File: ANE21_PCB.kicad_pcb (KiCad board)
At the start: 4 copper layers, 74.6 x 59.6 mm, 60 parts, among them J1 Conn_02x05_Odd_Even, J13 1-2199119-5, J15 USB_OTG, J16 Conn_01x02, J2 Barrel_Jack, J3 USB-A-S-VT, J4 THD-20-R, J5 690-019-298-412, J6 SS-52400-004, U1 74LVC1G07SE-7, U10 PUSB3FR4, U11 TPD4EUSB30, U12 SI-51005-F, U13 RT9742SNGV, U2 74LVC1G07SE-7, U3 HUSB238_xxxDD, U4 AP62300WU-7, U8 AP62300WU-7, U9 PUSB3FR4

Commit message: heb de GPIO aangepast.
Laten we morgen de stand van zaken bespreken. En overleggen wat we kunnen doen
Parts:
- added R7: 10k, Resistor_SMD:R_0402_1005Metric_Pad0.72x0.64mm_HandSolder, F.Cu at (1.14, 0.49)
- moved J4 225.2 mm to (117.7, 130.5), turned to -90 degrees
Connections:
- J4 pad 1: +3,3V DC -> 3.3V OUT (CM4.84)
- J4 pad 10: /CM4_LowSpeed/GPIO15 -> /CM4_LowSpeed/GPIO7
- J4 pad 11: /CM4_LowSpeed/GPIO17 -> /CM4_LowSpeed/GPIO8
- J4 pad 12: /CM4_LowSpeed/GPIO18 -> /CM4_LowSpeed/GPIO9
- J4 pad 13: /CM4_LowSpeed/GPIO27 -> /CM4_LowSpeed/GPIO10
- J4 pad 14: GND -> /CM4_LowSpeed/GPIO11
- J4 pad 15: /CM4_LowSpeed/GPIO22 -> /CM4_LowSpeed/GPIO12
- J4 pad 16: /CM4_LowSpeed/GPIO23 -> /CM4_LowSpeed/GPIO13
- J4 pad 17: +3,3V DC -> /CM4_LowSpeed/GPIO14
- J4 pad 18: /CM4_LowSpeed/GPIO24 -> /CM4_LowSpeed/GPIO15
- J4 pad 19: /CM4_LowSpeed/GPIO10 -> /CM4_LowSpeed/GPIO16
- J4 pad 2: /CM4_LowSpeed/+5v -> 1.8V OUT (CM4.90)
- J4 pad 20: GND -> /CM4_LowSpeed/GPIO17
- J4 pad 21: /CM4_LowSpeed/GPIO9 -> /CM4_LowSpeed/GPIO18
- J4 pad 22: /CM4_LowSpeed/GPIO25 -> /CM4_LowSpeed/GPIO19
- J4 pad 23: /CM4_LowSpeed/GPIO11 -> /CM4_LowSpeed/GPIO20
- J4 pad 24: /CM4_LowSpeed/GPIO8 -> /CM4_LowSpeed/GPIO21
- J4 pad 25: GND -> /CM4_LowSpeed/GPIO22
- J4 pad 26: /CM4_LowSpeed/GPIO7 -> /CM4_LowSpeed/GPIO23
- J4 pad 27: /CM4_LowSpeed/ID_SD -> /CM4_LowSpeed/GPIO24
- J4 pad 28: /CM4_LowSpeed/ID_SC -> /CM4_LowSpeed/GPIO25
- J4 pad 29: /CM4_LowSpeed/GPIO5 -> /CM4_LowSpeed/GPIO26
- J4 pad 3: /CM4_LowSpeed/GPIO2 -> 3.3V OUT (CM4.86)
- J4 pad 30: GND -> /CM4_LowSpeed/GPIO27
- J4 pad 31: /CM4_LowSpeed/GPIO6 -> /CM4_LowSpeed/WL_nDis
- J4 pad 32: /CM4_LowSpeed/GPIO12 -> unconnected-(J4-Pin_32-Pad32)
- J4 pad 33: /CM4_LowSpeed/GPIO13 -> /CM4_LowSpeed/BT_nDis
- J4 pad 34: GND -> unconnected-(J4-Pin_34-Pad34)
- J4 pad 35: /CM4_LowSpeed/GPIO19 -> /CM4_LowSpeed/nRPIBOOT
- J4 pad 36: /CM4_LowSpeed/GPIO16 -> unconnected-(J4-Pin_36-Pad36)
- J4 pad 37: /CM4_LowSpeed/GPIO26 -> /CM4_LowSpeed/ID_SD
- J4 pad 38: /CM4_LowSpeed/GPIO20 -> /CM4_LowSpeed/ID_SC
- J4 pad 4: /CM4_LowSpeed/+5v -> 1.8V OUT (CM4.88)
- J4 pad 40: /CM4_LowSpeed/GPIO21 -> GND
- J4 pad 5: /CM4_LowSpeed/GPIO3 -> /CM4_LowSpeed/GPIO2
- J4 pad 6: GND -> /CM4_LowSpeed/GPIO3
- J4 pad 8: /CM4_LowSpeed/GPIO14 -> /CM4_LowSpeed/GPIO5
- J4 pad 9: GND -> /CM4_LowSpeed/GPIO6
- Module1 pad 20: unconnected-(Module1A-EEPROM_nWP-Pad20) -> Net-(Module1A-EEPROM_nWP)
- Module1 pad 24: unconnected-(Module1A-GPIO26-Pad24) -> /CM4_LowSpeed/GPIO26
- Module1 pad 25: unconnected-(Module1A-GPIO21-Pad25) -> /CM4_LowSpeed/GPIO21
- Module1 pad 26: unconnected-(Module1A-GPIO19-Pad26) -> /CM4_LowSpeed/GPIO19
- Module1 pad 27: unconnected-(Module1A-GPIO20-Pad27) -> /CM4_LowSpeed/GPIO20
- Module1 pad 28: unconnected-(Module1A-GPIO13-Pad28) -> /CM4_LowSpeed/GPIO13
- Module1 pad 29: unconnected-(Module1A-GPIO16-Pad29) -> /CM4_LowSpeed/GPIO16
- Module1 pad 30: unconnected-(Module1A-GPIO6-Pad30) -> /CM4_LowSpeed/GPIO6
- Module1 pad 31: unconnected-(Module1A-GPIO12-Pad31) -> /CM4_LowSpeed/GPIO12
- Module1 pad 34: unconnected-(Module1A-GPIO5-Pad34) -> /CM4_LowSpeed/GPIO5
- Module1 pad 35: unconnected-(Module1A-ID_SC-Pad35) -> /CM4_LowSpeed/ID_SC
- Module1 pad 36: unconnected-(Module1A-ID_SD-Pad36) -> /CM4_LowSpeed/ID_SD
- Module1 pad 37: unconnected-(Module1A-GPIO7-Pad37) -> /CM4_LowSpeed/GPIO7
- Module1 pad 38: unconnected-(Module1A-GPIO11-Pad38) -> /CM4_LowSpeed/GPIO11
- Module1 pad 39: unconnected-(Module1A-GPIO8-Pad39) -> /CM4_LowSpeed/GPIO8
- Module1 pad 40: unconnected-(Module1A-GPIO9-Pad40) -> /CM4_LowSpeed/GPIO9
- Module1 pad 41: unconnected-(Module1A-GPIO25-Pad41) -> /CM4_LowSpeed/GPIO25
- Module1 pad 44: unconnected-(Module1A-GPIO10-Pad44) -> /CM4_LowSpeed/GPIO10
- Module1 pad 45: unconnected-(Module1A-GPIO24-Pad45) -> /CM4_LowSpeed/GPIO24
- Module1 pad 46: unconnected-(Module1A-GPIO22-Pad46) -> /CM4_LowSpeed/GPIO22
- Module1 pad 47: unconnected-(Module1A-GPIO23-Pad47) -> /CM4_LowSpeed/GPIO23
- Module1 pad 48: unconnected-(Module1A-GPIO27-Pad48) -> /CM4_LowSpeed/GPIO27
- Module1 pad 49: unconnected-(Module1A-GPIO18-Pad49) -> /CM4_LowSpeed/GPIO18
- Module1 pad 50: unconnected-(Module1A-GPIO17-Pad50) -> /CM4_LowSpeed/GPIO17
- Module1 pad 51: unconnected-(Module1A-GPIO15-Pad51) -> /CM4_LowSpeed/GPIO15
- Module1 pad 54: unconnected-(Module1A-GPIO4-Pad54) -> /CM4_LowSpeed/GPIO4
- Module1 pad 55: unconnected-(Module1A-GPIO14-Pad55) -> /CM4_LowSpeed/GPIO14
- Module1 pad 56: unconnected-(Module1A-GPIO3-Pad56) -> /CM4_LowSpeed/GPIO3
- Module1 pad 58: unconnected-(Module1A-GPIO2-Pad58) -> /CM4_LowSpeed/GPIO2
- Module1 pad 84: +3,3V DC -> 3.3V OUT (CM4.84)
- Module1 pad 86: +3,3V DC -> 3.3V OUT (CM4.86)
- Module1 pad 88: /CM4_LowSpeed/+1.8v -> 1.8V OUT (CM4.88)
- Module1 pad 90: /CM4_LowSpeed/+1.8v -> 1.8V OUT (CM4.90)

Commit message: Added HDMI traces but have not checked them
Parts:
- moved R7 129.8 mm to (75.3, 107.0)
- moved C14 45.8 mm to (118.6, 76.8)
- moved R15 0.74 mm to (131.4, 81.2), turned to 0 degrees
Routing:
- net /CM4_LowSpeed/E7: track 0.00 -> 11.2 mm
- net /CM4_LowSpeed/E5: track 0.00 -> 10.7 mm
- net /CM4_HighSpeed/HDMI0_D2_P: track 0.00 -> 10.6 mm
- net /CM4_HighSpeed/HDMI0_D2_N: track 0.00 -> 10.6 mm
- net /CM4_LowSpeed/E2: track 0.00 -> 10.5 mm
- net /CM4_LowSpeed/E4: track 0.00 -> 10.3 mm
- net /CM4_HighSpeed/HDMI0_D1_P: track 0.00 -> 10.1 mm
- net /CM4_HighSpeed/HDMI0_D1_N: track 0.00 -> 10.1 mm
- net /CM4_HighSpeed/HDMI0_D0_P: track 0.00 -> 9.91 mm
- net /CM4_HighSpeed/HDMI0_D0_N: track 0.00 -> 9.91 mm
- net /CM4_HighSpeed/HDMI0_CK_P: track 0.00 -> 9.78 mm
- net /CM4_HighSpeed/HDMI0_CK_N: track 0.00 -> 9.78 mm
- net /CM4_LowSpeed/E8: track 0.00 -> 8.95 mm
- net /CM4_LowSpeed/E6: track 0.00 -> 8.52 mm
- net /CM4_LowSpeed/E1: track 0.00 -> 7.71 mm
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
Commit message: Added lots and lots of traces in PCB design.
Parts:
- removed J4: THD-20-R, Connector_PinHeader_2.54mm:PinHeader_2x20_P2.54mm_Vertical
- removed J6: SS-52400-004, SS-52400-004 (USB-c connector):STEWART_SS-52400-004 (USB-C)
- added J7: 2036150003 (USB-C_Connector), USB-C:CONN_2036150003_MOL(USB-c_connector), F.Cu at (115.1, 53.1)
- moved C3 85.9 mm to (108.4, 58.2), turned to 90 degrees
- moved C2 84.7 mm to (107.3, 58.2), turned to 90 degrees
- moved C1 83.4 mm to (106.3, 58.2), turned to 90 degrees
- moved U3 80.0 mm to (107.0, 55.3), turned to 180 degrees
- moved R1 78.7 mm to (103.6, 54.1), turned to 90 degrees
- moved R2 78.6 mm to (103.6, 56.5), turned to -90 degrees
- moved J3 30.9 mm to (120.7, 82.1), turned to 90 degrees
- moved U11 21.7 mm to (117.6, 77.8)
- moved C14 18.5 mm to (119.1, 58.3), turned to 180 degrees
- moved J15 16.7 mm to (130.0, 78.3)
- moved J2 13.0 mm to (129.3, 61.5), turned to 180 degrees
- moved J16 12.2 mm to (131.1, 71.5), turned to -90 degrees
- moved U9 8.93 mm to (128.2, 90.0)
- moved U12 8.88 mm to (126.0, 105.8)
- moved R15 8.87 mm to (131.6, 90.1)
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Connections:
- net /CM4_LowSpeed/E1 renamed /CM4_LowSpeed/TRD0_P
- net /CM4_LowSpeed/E10 renamed /CM4_LowSpeed/LEDY
- net /CM4_LowSpeed/E2 renamed /CM4_LowSpeed/TRD0_N
- net /CM4_LowSpeed/E5 renamed /CM4_LowSpeed/TRD2_P
- net /CM4_LowSpeed/E6 renamed /CM4_LowSpeed/TRD2_N
- net /CM4_LowSpeed/E7 renamed /CM4_LowSpeed/TRD3_P
- net /CM4_LowSpeed/E8 renamed /CM4_LowSpeed/TRD3_N
- net /CM4_LowSpeed/E9 renamed /CM4_LowSpeed/LEDG
- J13 pad 50: +3,3V DC -> /CM4_HighSpeed/P_RST
- J13 pad 52: +3,3V DC -> /CM4_HighSpeed/P_CLKnREQ
- Module1 pad 102: +3,3V DC -> /CM4_HighSpeed/P_CLKnREQ
- Module1 pad 109: +3,3V DC -> /CM4_HighSpeed/P_RST
- Module1 pad 4: /CM4_LowSpeed/E3 -> /CM4_LowSpeed/TRD1_N
- Module1 pad 6: /CM4_LowSpeed/E4 -> /CM4_LowSpeed/TRD1_P
- U12 pad 4: /CM4_LowSpeed/E3 -> /CM4_LowSpeed/TRD1_P
- U12 pad 5: /CM4_LowSpeed/E4 -> /CM4_LowSpeed/TRD1_N
- U9 pad 1: /CM4_LowSpeed/E4 -> /CM4_LowSpeed/TRD1_N
- U9 pad 10: /CM4_LowSpeed/E4 -> /CM4_LowSpeed/TRD1_N
- U9 pad 2: /CM4_LowSpeed/E3 -> /CM4_LowSpeed/TRD1_P
- U9 pad 9: /CM4_LowSpeed/E3 -> /CM4_LowSpeed/TRD1_P
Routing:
- net +3,3V DC: track 0.00 -> 124.0 mm, vias 0 -> 3
- net /CM4_LowSpeed/TRD1_N: track 0.00 -> 72.6 mm
- net /CM4_LowSpeed/TRD1_P: track 0.00 -> 70.1 mm
- net /CM4_LowSpeed/LEDG: track 0.00 -> 63.0 mm, vias 0 -> 2
- net USB_OTG: track 0.00 -> 59.4 mm, vias 0 -> 2
- net /CM4_LowSpeed/TRD2_N: track 8.52 -> 67.0 mm, vias 0 -> 1
- net /CM4_LowSpeed/TRD2_P: track 10.7 -> 67.4 mm, vias 0 -> 1
- net +5V DC: track 0.00 -> 56.6 mm, vias 0 -> 5
- net /CM4_LowSpeed/TRD0_P: track 7.71 -> 62.4 mm, vias 0 -> 1
- net VIN_U9: track 0.00 -> 54.5 mm, vias 0 -> 4
- net /CM4_LowSpeed/TRD3_P: track 11.2 -> 64.7 mm
- net /CM4_LowSpeed/TRD3_N: track 8.95 -> 61.8 mm
- net /CM4_LowSpeed/TRD0_N: track 10.5 -> 61.8 mm, vias 0 -> 1
- net GND: track 0.00 -> 49.7 mm, vias 0 -> 34
- net /CM4_LowSpeed/LEDY: track 0.00 -> 42.3 mm
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- added copper zone on In2.Cu, net +5V DC
- added copper zone on In1.Cu, net GND
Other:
- board size 74.6 x 59.6 mm -> 74.6 x 59.4 mm

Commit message: PCB is af. kan je het nog checken?
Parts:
- moved J1 92.0 mm to (62.9, 112.5), turned to 90 degrees
- moved U1 72.2 mm to (63.5, 106.7), turned to 180 degrees
- moved R23 0.43 mm to (86.1, 105.5)
- moved D3 0.28 mm to (85.7, 107.0)
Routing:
- net GND: track 49.7 -> 459.5 mm, vias 34 -> 45
- net +3,3V DC: track 124.0 -> 204.9 mm, vias 3 -> 4
- net +5V DC: track 56.6 -> 89.6 mm
- net Net-(J1-Pin_1): track 0.00 -> 8.06 mm
- net Net-(D3-K): track 4.19 -> 4.77 mm
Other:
- board size 74.6 x 59.4 mm -> 74.6 x 66 mm

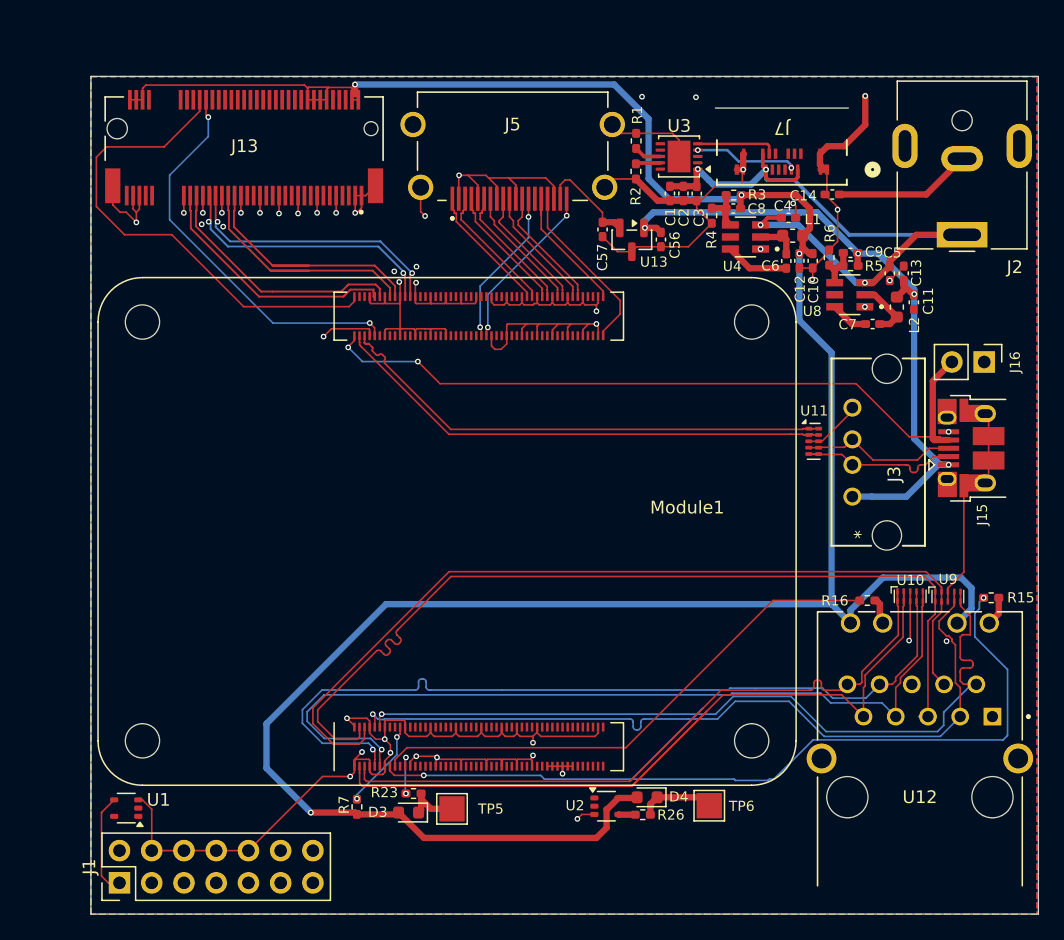
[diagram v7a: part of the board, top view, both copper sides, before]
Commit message: Redid the routing and fixed ERC warnings
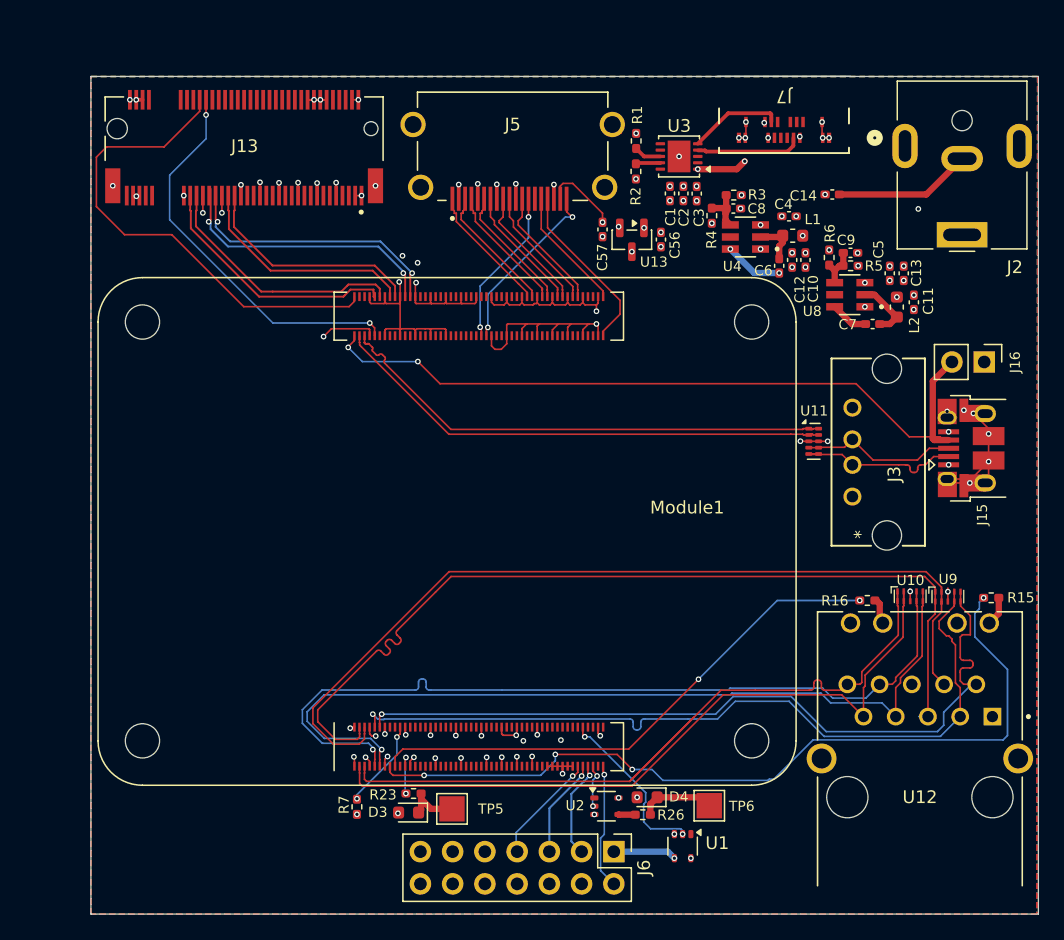
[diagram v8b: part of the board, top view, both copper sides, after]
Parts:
- removed J1: Conn_02x05_Odd_Even, Connector_PinHeader_2.54mm:PinHeader_2x07_P2.54mm_Vertical
- added J6: Conn_02x07_Odd_Even, Connector_PinHeader_2.54mm:PinHeader_2x07_P2.54mm_Vertical, F.Cu at (101.9, 110.1)
- moved U1 43.9 mm to (107.3, 109.6), turned to -90 degrees
- moved J7 2.50 mm to (115.3, 50.6)
- moved C6 0.67 mm to (114.9, 63.9)
- moved C10 0.57 mm to (117.0, 63.5)
- moved C12 0.57 mm to (115.9, 63.5)
- moved C4 0.14 mm to (115.7, 60.0)
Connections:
- net +3,3V DC renamed /+3.3v
- net VIN_U9 renamed /+12v
- C11 pad 2: +5V DC -> /+5v
- C13 pad 2: +5V DC -> /+5v
- C56 pad 1: +5V DC -> /+5v
- C9 pad 2: +5V DC -> /+5v
- J15 pad 1: +5V DC -> /+5v
- J3 pad 1: +5V DC -> /+5v
- L2 pad 2: +5V DC -> /+5v
- Module1 pad 77: +5V DC -> /+5v
- Module1 pad 79: +5V DC -> /+5v
- Module1 pad 81: +5V DC -> /+5v
- Module1 pad 83: +5V DC -> /+5v
- Module1 pad 85: +5V DC -> /+5v
- Module1 pad 87: +5V DC -> /+5v
- R5 pad 1: +5V DC -> /+5v
- U1 pad 2: /RUN_PG -> /CM4_LowSpeed/RUN_PG
- U13 pad 1: +5V DC -> /+5v
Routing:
- net GND: track 459.5 -> 188.6 mm, vias 45 -> 87
- net +5V DC: track 89.6 -> 0.00 mm, vias 5 -> 0
- net /+5v: track 0.00 -> 36.1 mm, vias 0 -> 10
- net /+3.3v: track 204.9 -> 177.2 mm, vias 4 -> 14
- net /CM4_LowSpeed/RUN_PG: track 0.00 -> 13.5 mm, vias 0 -> 2
- net /CM4_LowSpeed/GLOBAL_EN: track 0.00 -> 10.0 mm, vias 0 -> 1
- net /+12v: track 54.5 -> 45.3 mm, vias 4 -> 12
- net /CM4_LowSpeed/WL_nDis: track 0.00 -> 8.96 mm, vias 0 -> 1
- net /CM4_LowSpeed/TRD3_P: track 64.7 -> 56.4 mm
- net /CM4_LowSpeed/BT_nDis: track 0.00 -> 7.82 mm, vias 0 -> 1
- net /CM4_LowSpeed/nRPIBOOT: track 0.00 -> 7.74 mm, vias 0 -> 1
- net /CM4_LowSpeed/nPWR_LED: track 0.00 -> 3.58 mm, vias 0 -> 2
- net Net-(J6-Pin_1): track 8.06 -> 4.98 mm, vias 0 -> 1
- net /CM4_HighSpeed/P_RX0_P: track 21.0 -> 18.0 mm
- net /CM4_HighSpeed/P_RX0_N: track 20.8 -> 18.0 mm
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- added copper zone on In2.Cu, net /+5v
- added copper zone on B.Cu, net /CM4_HighSpeed/HDMI0_CK_N
- added copper zone on F.Cu, net /CM4_HighSpeed/HDMI0_CK_N
- removed copper zone on In2.Cu, net +5V DC
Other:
- rule pad_to_mask_clearance: 0 -> 0.05
